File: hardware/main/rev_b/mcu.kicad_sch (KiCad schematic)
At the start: 23 parts, among them J10 SWD, U10 RP2354B, Y1 12MHz ABM8-272-T3

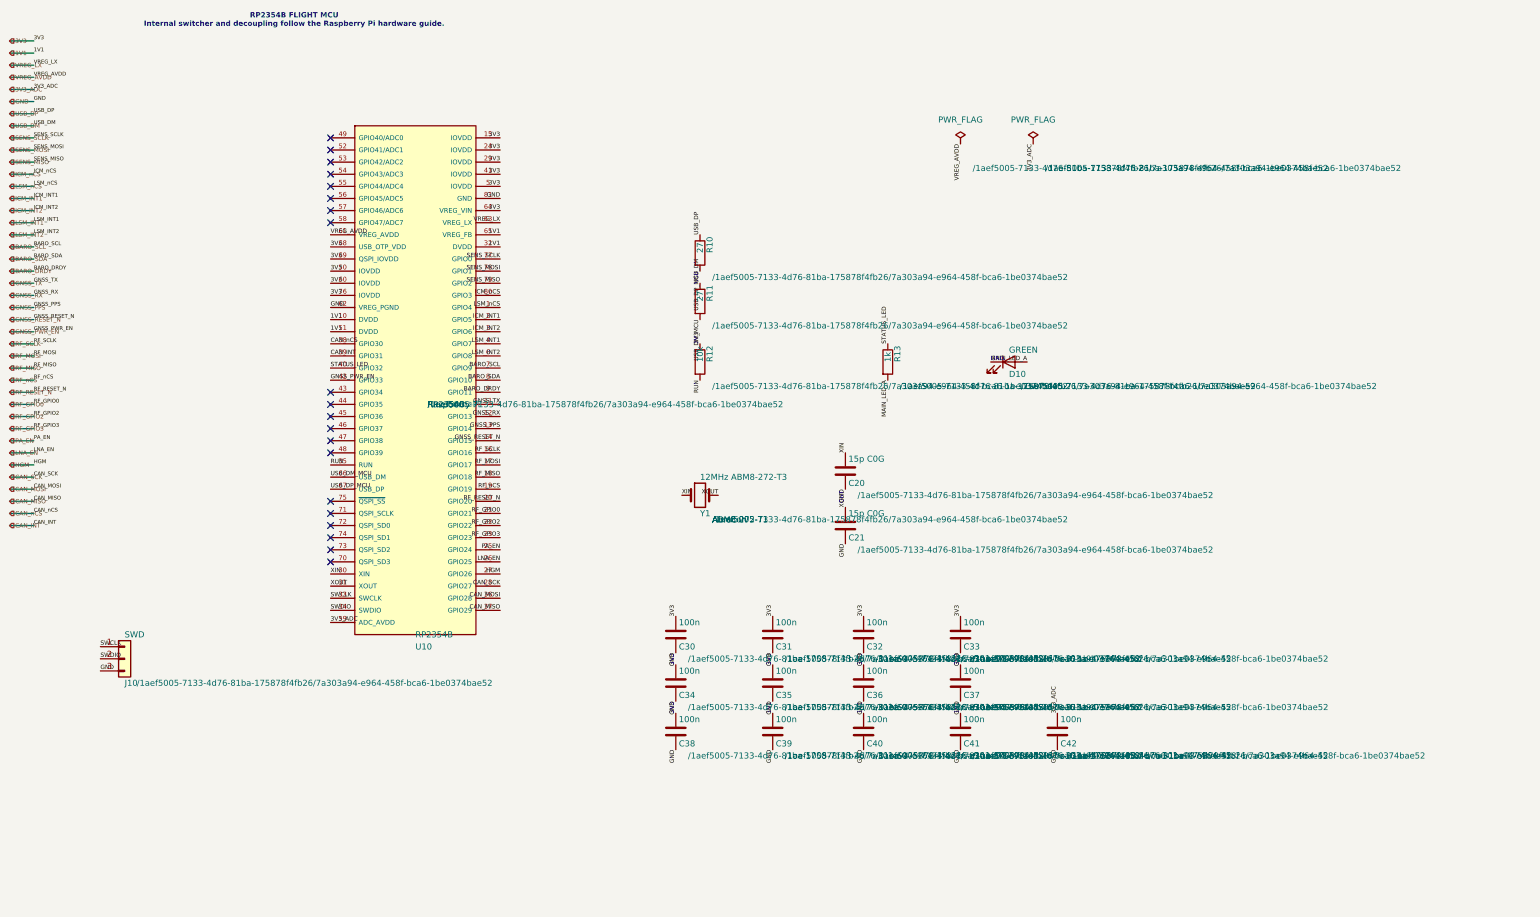
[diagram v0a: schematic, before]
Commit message: Add Main Rev B ESC interfaces
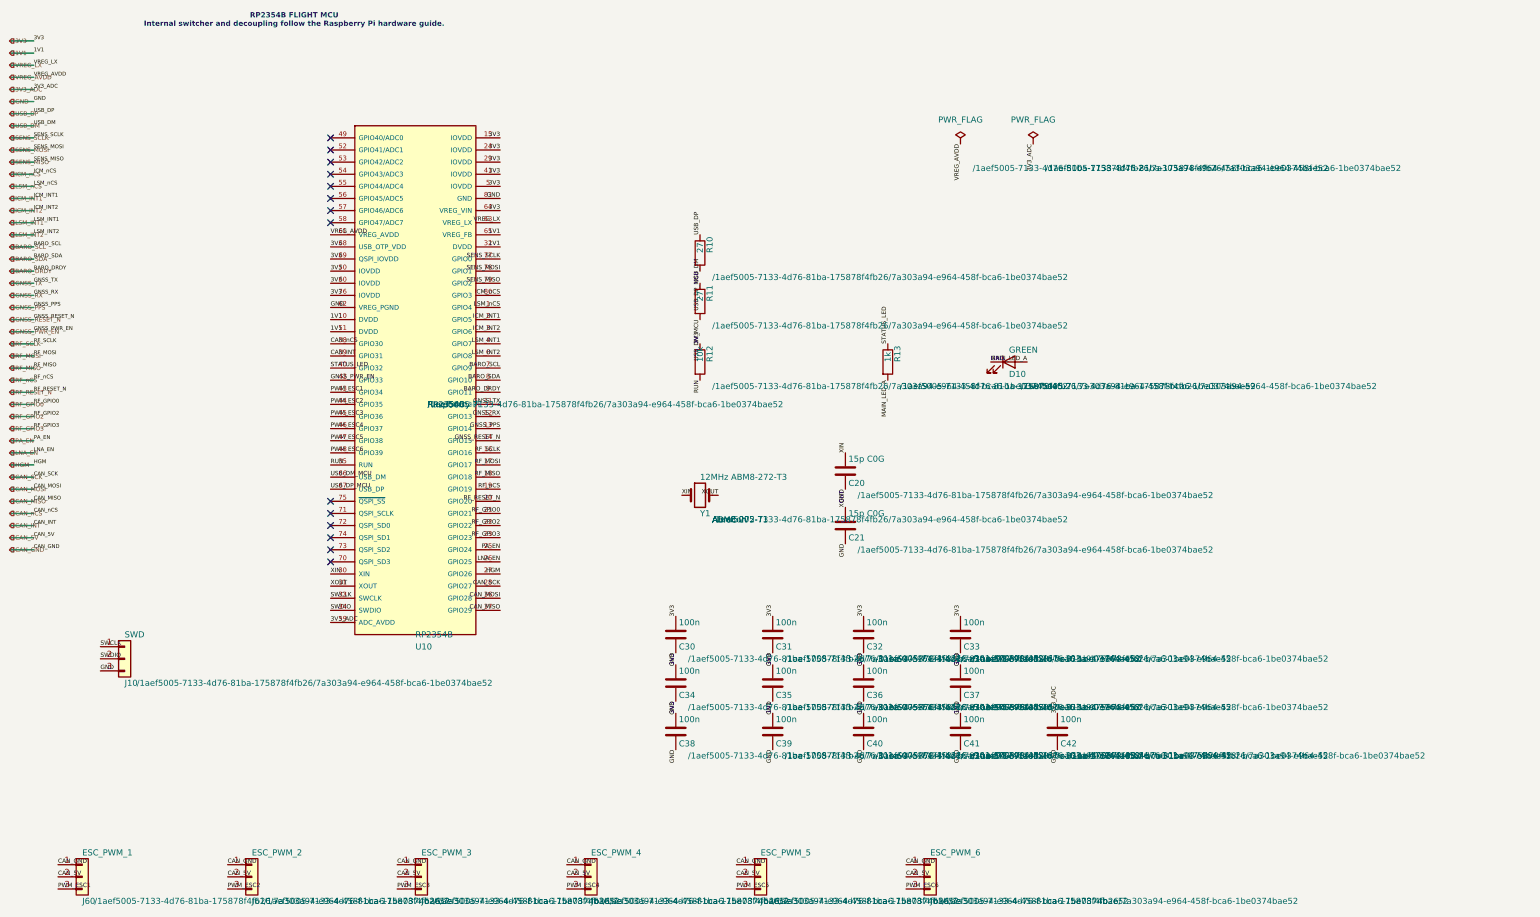
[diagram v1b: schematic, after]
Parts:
- added J60: ESC_PWM_1, Connector_PinHeader_2.54mm:PinHeader_1x03_P2.54mm_Vertical, symbol Connector_Generic:Conn_01x03
- added J61: ESC_PWM_2, Connector_PinHeader_2.54mm:PinHeader_1x03_P2.54mm_Vertical, symbol Connector_Generic:Conn_01x03
- added J62: ESC_PWM_3, Connector_PinHeader_2.54mm:PinHeader_1x03_P2.54mm_Vertical, symbol Connector_Generic:Conn_01x03
- added J63: ESC_PWM_4, Connector_PinHeader_2.54mm:PinHeader_1x03_P2.54mm_Vertical, symbol Connector_Generic:Conn_01x03
- added J64: ESC_PWM_5, Connector_PinHeader_2.54mm:PinHeader_1x03_P2.54mm_Vertical, symbol Connector_Generic:Conn_01x03
- added J65: ESC_PWM_6, Connector_PinHeader_2.54mm:PinHeader_1x03_P2.54mm_Vertical, symbol Connector_Generic:Conn_01x03
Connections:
- net PWM_ESC1: now reaches U10.43 (GPIO34)
- net PWM_ESC1: now also J60.3 (Pin_3)
- net PWM_ESC2: now reaches U10.44 (GPIO35)
- net PWM_ESC2: now also J61.3 (Pin_3)
- net PWM_ESC3: now reaches U10.45 (GPIO36)
- net PWM_ESC3: now also J62.3 (Pin_3)
- net PWM_ESC4: now reaches U10.46 (GPIO37)
- net PWM_ESC4: now also J63.3 (Pin_3)
- net PWM_ESC5: now reaches U10.47 (GPIO38)
- net PWM_ESC5: now also J64.3 (Pin_3)
- net PWM_ESC6: now reaches U10.48 (GPIO39)
- net PWM_ESC6: now also J65.3 (Pin_3)
- new net CAN_5V: J60.2 (Pin_2), J61.2 (Pin_2), J62.2 (Pin_2), J63.2 (Pin_2), J64.2 (Pin_2), J65.2 (Pin_2)
- new net CAN_GND: J60.1 (Pin_1), J61.1 (Pin_1), J62.1 (Pin_1), J63.1 (Pin_1), J64.1 (Pin_1), J65.1 (Pin_1)
- no-connect marks 20 -> 14
